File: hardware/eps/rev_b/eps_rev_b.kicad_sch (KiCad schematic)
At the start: 0 parts

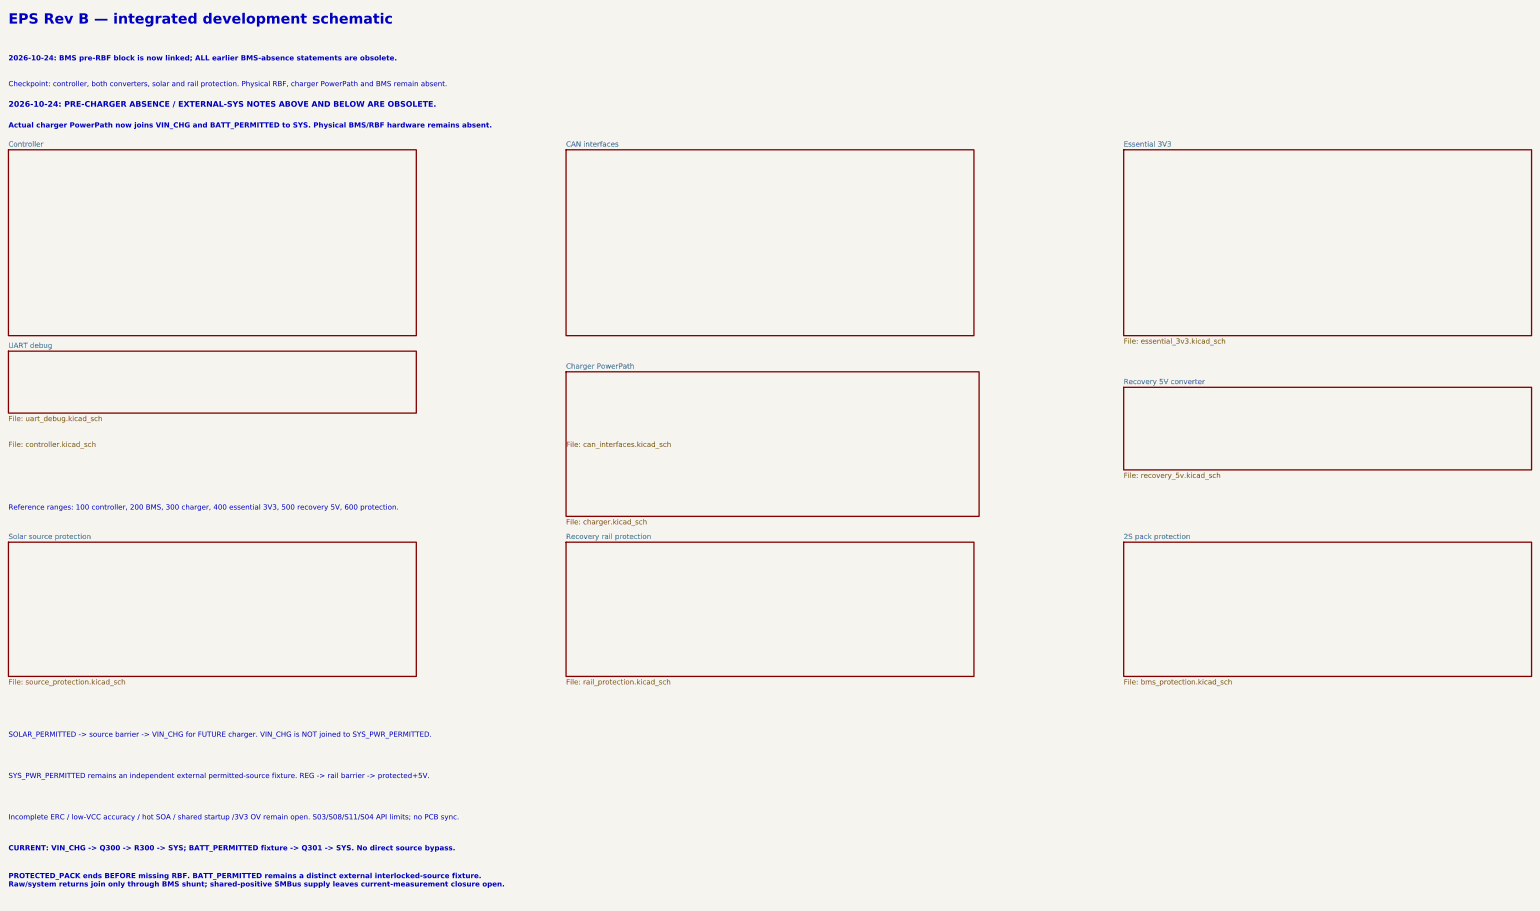
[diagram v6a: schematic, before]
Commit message: Integrate isolated BMS supply and MCU branch recovery controls
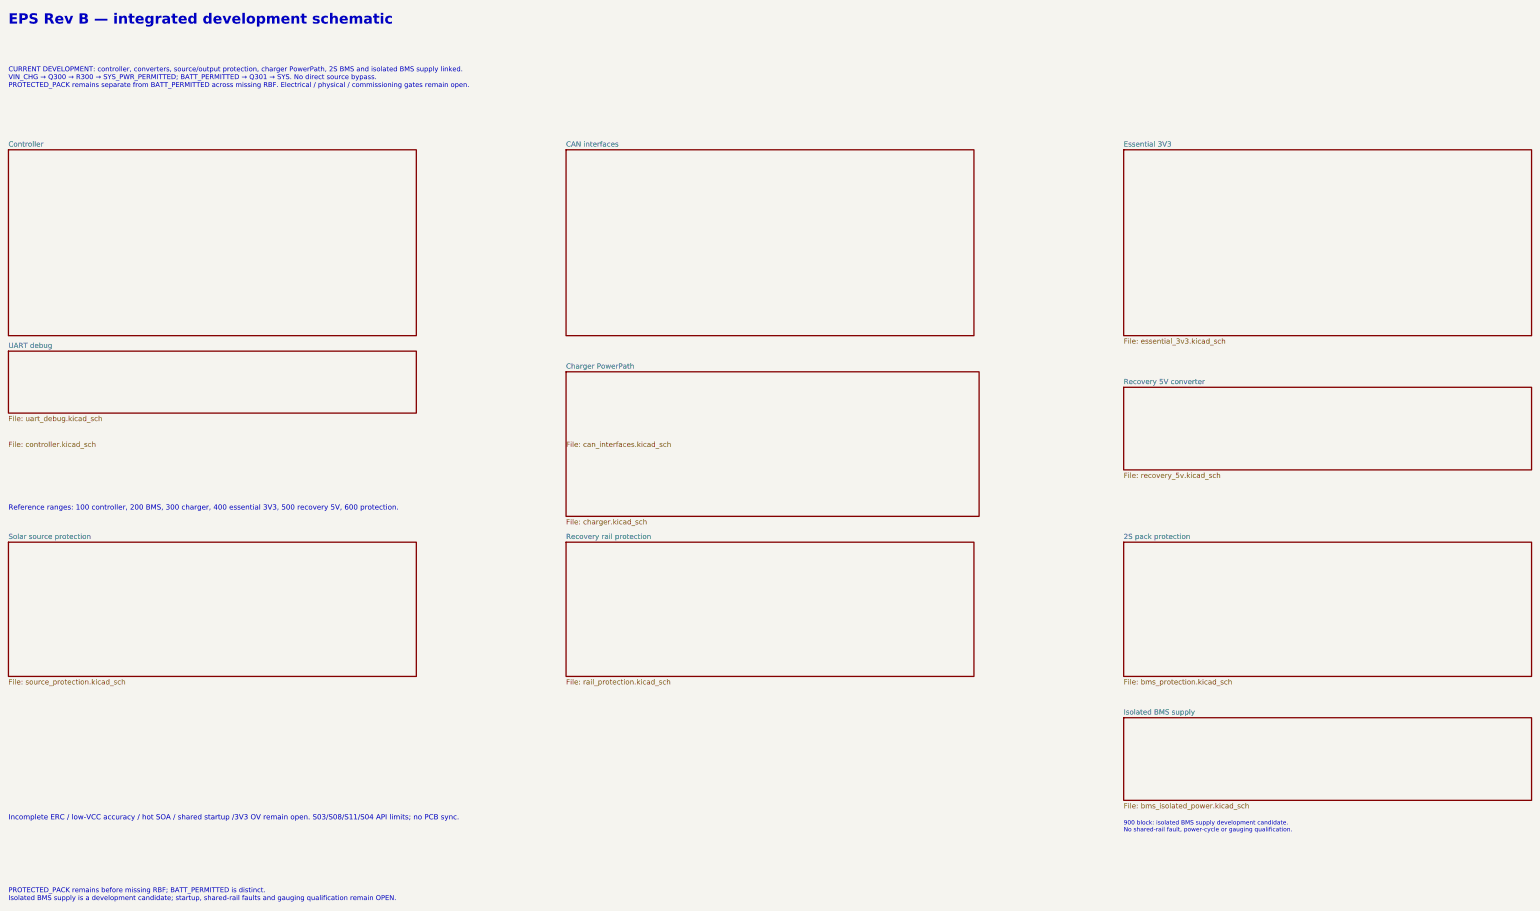
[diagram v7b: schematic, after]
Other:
- added sheet Isolated BMS supply (bms_isolated_power.kicad_sch)
- note added: "900 block: isolated BMS supply development candidate. No shared-rail fault, power-cycle or gauging qualification."
- note added: "CURRENT DEVELOPMENT: controller, converters, source/output protection, charger PowerPath, 2S BMS and isolated BMS supply linked. VIN_CHG → Q300 → R300 → SYS_PWR_PERMITTED; BATT_PERMITTED → Q301 → SYS. No direct source bypass. PROTECTED_PACK remains separate from BATT_PERMITTED across missing RBF. Electrical / physical / commissioning gates remain open."
- note added: "PROTECTED_PACK remains before missing RBF; BATT_PERMITTED is distinct. Isolated BMS supply is a development candidate; startup, shared-rail faults and gauging qualification remain OPEN."
- note removed: "2026-10-24: BMS pre-RBF block is now linked; ALL earlier BMS-absence statements are obsolete."
- note removed: "2026-10-24: PRE-CHARGER ABSENCE / EXTERNAL-SYS NOTES ABOVE AND BELOW ARE OBSOLETE."
- note removed: "Actual charger PowerPath now joins VIN_CHG and BATT_PERMITTED to SYS. Physical BMS/RBF hardware remains absent."
- note removed: "CURRENT: VIN_CHG -> Q300 -> R300 -> SYS; BATT_PERMITTED fixture -> Q301 -> SYS. No direct source bypass."
- note removed: "Checkpoint: controller, both converters, solar and rail protection. Physical RBF, charger PowerPath and BMS remain absent."
- note removed: "PROTECTED_PACK ends BEFORE missing RBF. BATT_PERMITTED remains a distinct external interlocked-source fixture. Raw/system returns join only through BMS shunt; shared-positive SMBus supply leaves current-measurement closure open."
- note removed: "SOLAR_PERMITTED -> source barrier -> VIN_CHG for FUTURE charger. VIN_CHG is NOT joined to SYS_PWR_PERMITTED."
- note removed: "SYS_PWR_PERMITTED remains an independent external permitted-source fixture. REG -> rail barrier -> protected+5V."
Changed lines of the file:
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@@
     )
-  )
-  (text "Checkpoint: controller, both converters, solar and rail protection. Physical RBF, charger PowerPath and BMS remain absent."
-    (at 30.48 45.72 0)
-    (effects (font (size 1.27 1.27)) (justify left bottom))
-  )
-  (text "SOLAR_PERMITTED -> source barrier -> VIN_CHG for FUTURE charger. VIN_CHG is NOT joined to SYS_PWR_PERMITTED."
-    (at 30.48 205.74 0)
-    (effects (font (size 1.27 1.27)) (justify left bottom))
-  )
-  (text "SYS_PWR_PERMITTED remains an independent external permitted-source fixture. REG -> rail barrier -> protected+5V."
-    (at 30.48 215.9 0)
-    (effects (font (size 1.27 1.27)) (justify left bottom))
   )
   (text "Incomplete ERC / low-VCC accuracy / hot SOA / shared startup /3V3 OV remain open. S03/S08/S11/S04 API limits; no PCB sync."
@@
 		)
 	)
-  (text "2026-10-24: PRE-CHARGER ABSENCE / EXTERNAL-SYS NOTES ABOVE AND BELOW ARE OBSOLETE."
-    (at 30.48 50.8 0)
-    (effects (font (size 1.4 1.4) (bold yes)) (justify left bottom))
-  )
-  (text "Actual charger PowerPath now joins VIN_CHG and BATT_PERMITTED to SYS. Physical BMS/RBF hardware remains absent."
-    (at 30.48 55.88 0)
-    (effects (font (size 1.27 1.27) (bold yes)) (justify left bottom))
-  )
-  (text "CURRENT: VIN_CHG -> Q300 -> R300 -> SYS; BATT_PERMITTED fixture -> Q301 -> SYS. No direct source bypass."
-    (at 30.48 233.68 0)
-    (effects (font (size 1.27 1.27) (bold yes)) (justify left bottom))
-  )
 	(sheet
     (at 304.8 157.48)
@@
       )
     )
-  )
-  (text "2026-10-24: BMS pre-RBF block is now linked; ALL earlier BMS-absence statements are obsolete."
-    (at 30.48 39.37 0)
-    (effects (font (size 1.27 1.27) (bold yes)) (justify left bottom))
-  )
-  (text "PROTECTED_PACK ends BEFORE missing RBF. BATT_PERMITTED remains a distinct external interlocked-source fixture.\nRaw/system returns join only through BMS shunt; shared-positive SMBus supply leaves current-measurement closure open."
-    (at 30.48 242.57 0)
-    (effects (font (size 1.27 1.27) (bold yes)) (justify left bottom))
   )
 	(sheet
@@
     )
   )
+	(sheet
+    (at 304.8 200.66)
+    (size 100.33 20.32)
+    (fields_autoplaced yes)
+    (stroke (width 0.1524) (type solid))
+    (fill (color 0 0 0 0.0))
+    (property "Sheetname" "Isolated BMS supply"
+      (at 304.8 200.025 0)
+      (effects (font (size 1.27 1.27)) (justify left bottom))
+    )
+    (property "Sheetfile" "bms_isolated_power.kicad_sch"
+      (at 304.8 221.61499999999998 0)
+      (effects (font (size 1.27 1.27)) (justify left top))
+    )
+    (instances
+      (project "eps_rev_b"
+        (path "/8eba9f22-6f11-42d7-8e4a-b8de8905b113" (page "11"))
+      )
+    )
+  )
+  (text "PROTECTED_PACK remains before missing RBF; BATT_PERMITTED is distinct.\nIsolated BMS supply is a development candidate; startup, shared-rail faults and gauging qualification remain OPEN."
+    (at 30.48 242.57 0)
+    (effects (font (size 1.2 1.2)) (justify left top))
+  )
+  (text "900 block: isolated BMS supply development candidate.\nNo shared-rail fault, power-cycle or gauging qualification."
+    (at 304.8 226.06 0)
+    (effects (font (size 1.05 1.05)) (justify left top))
+  )
+  (text "CURRENT DEVELOPMENT: controller, converters, source/output protection, charger PowerPath, 2S BMS and isolated BMS supply linked.\nVIN_CHG → Q300 → R300 → SYS_PWR_PERMITTED; BATT_PERMITTED → Q301 → SYS. No direct source bypass.\nPROTECTED_PACK remains separate from BATT_PERMITTED across missing RBF. Electrical / physical / commissioning gates remain open."
+    (at 30.48 40.64 0)
+    (effects (font (size 1.2 1.2)) (justify left top))
+  )
 )

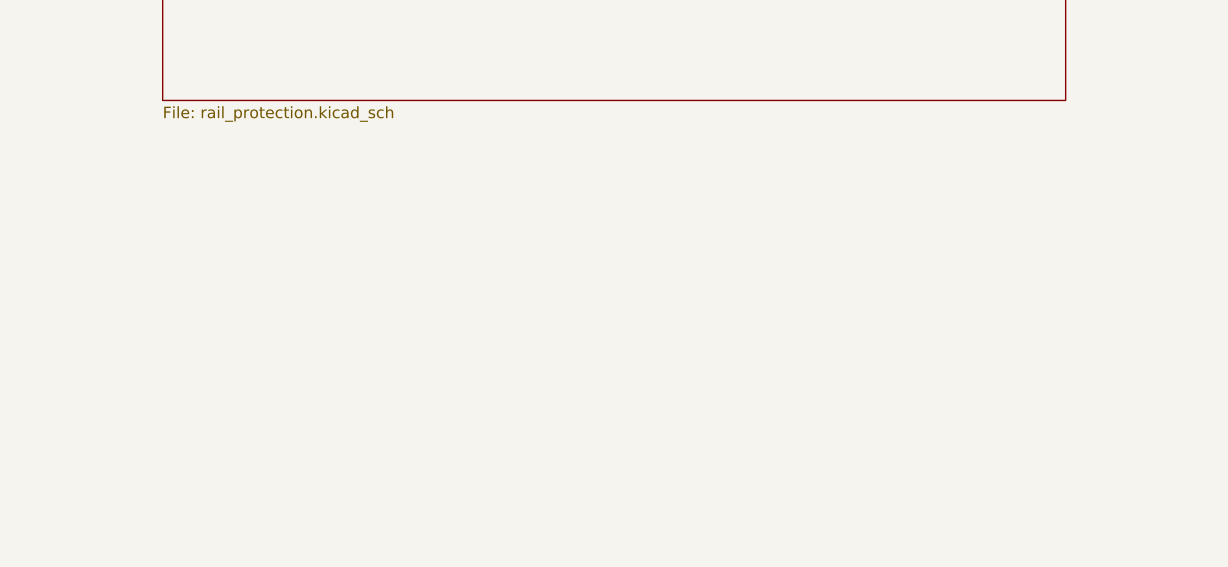
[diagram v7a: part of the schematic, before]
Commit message: Integrate independent CAN supplies and standby-controlled latch reset
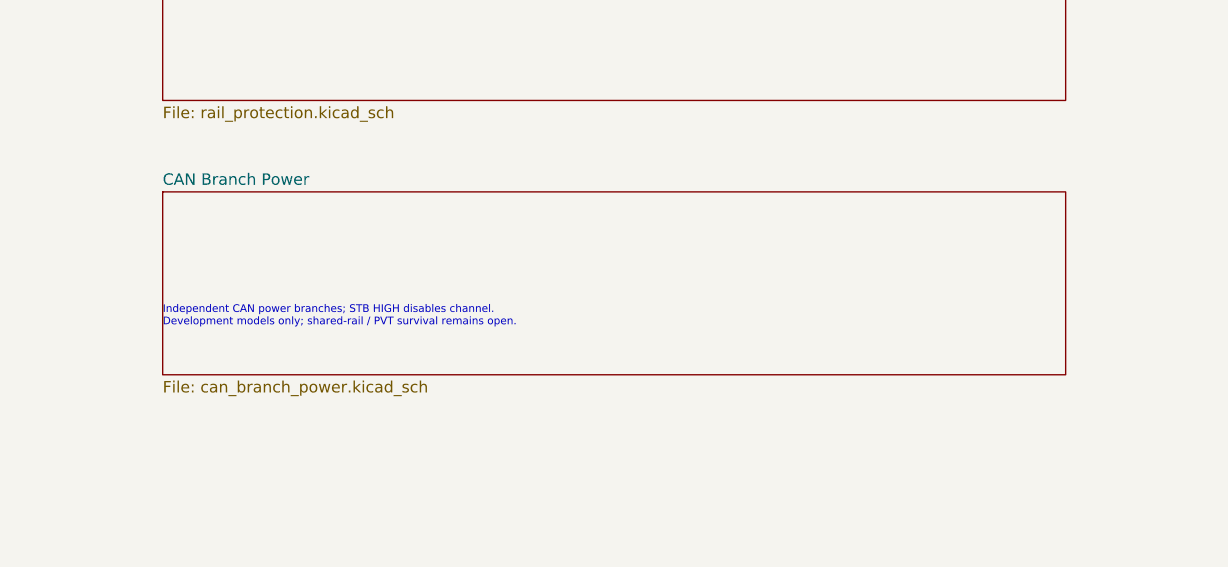
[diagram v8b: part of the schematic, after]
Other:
- added sheet CAN Branch Power (can_branch_power.kicad_sch)
- note added: "Independent CAN power branches; STB HIGH disables channel. Development models only; shared-rail / PVT survival remains open."
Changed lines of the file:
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@@
     (effects (font (size 1.2 1.2)) (justify left top))
   )
+	(sheet
+    (at 167.64 200.66)
+    (size 100.33 20.32)
+    (fields_autoplaced yes)
+    (stroke (width 0.1524) (type solid))
+    (fill (color 0 0 0 0.0))
+    (property "Sheetname" "CAN Branch Power"
+      (at 167.64 200.025 0)
+      (effects (font (size 1.27 1.27)) (justify left bottom))
+    )
+    (property "Sheetfile" "can_branch_power.kicad_sch"
+      (at 167.64 221.61499999999998 0)
+      (effects (font (size 1.27 1.27)) (justify left top))
+    )
+    (instances
+      (project "eps_rev_b"
+        (path "/8eba9f22-6f11-42d7-8e4a-b8de8905b113" (page "12"))
+      )
+    )
+  )
+  (text "Independent CAN power branches; STB HIGH disables channel.\nDevelopment models only; shared-rail / PVT survival remains open."
+    (at 167.64 213.36 0)
+    (effects (font (size 0.85 0.85)) (justify left top))
+  )
 )
